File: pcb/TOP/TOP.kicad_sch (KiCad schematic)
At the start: 90 parts

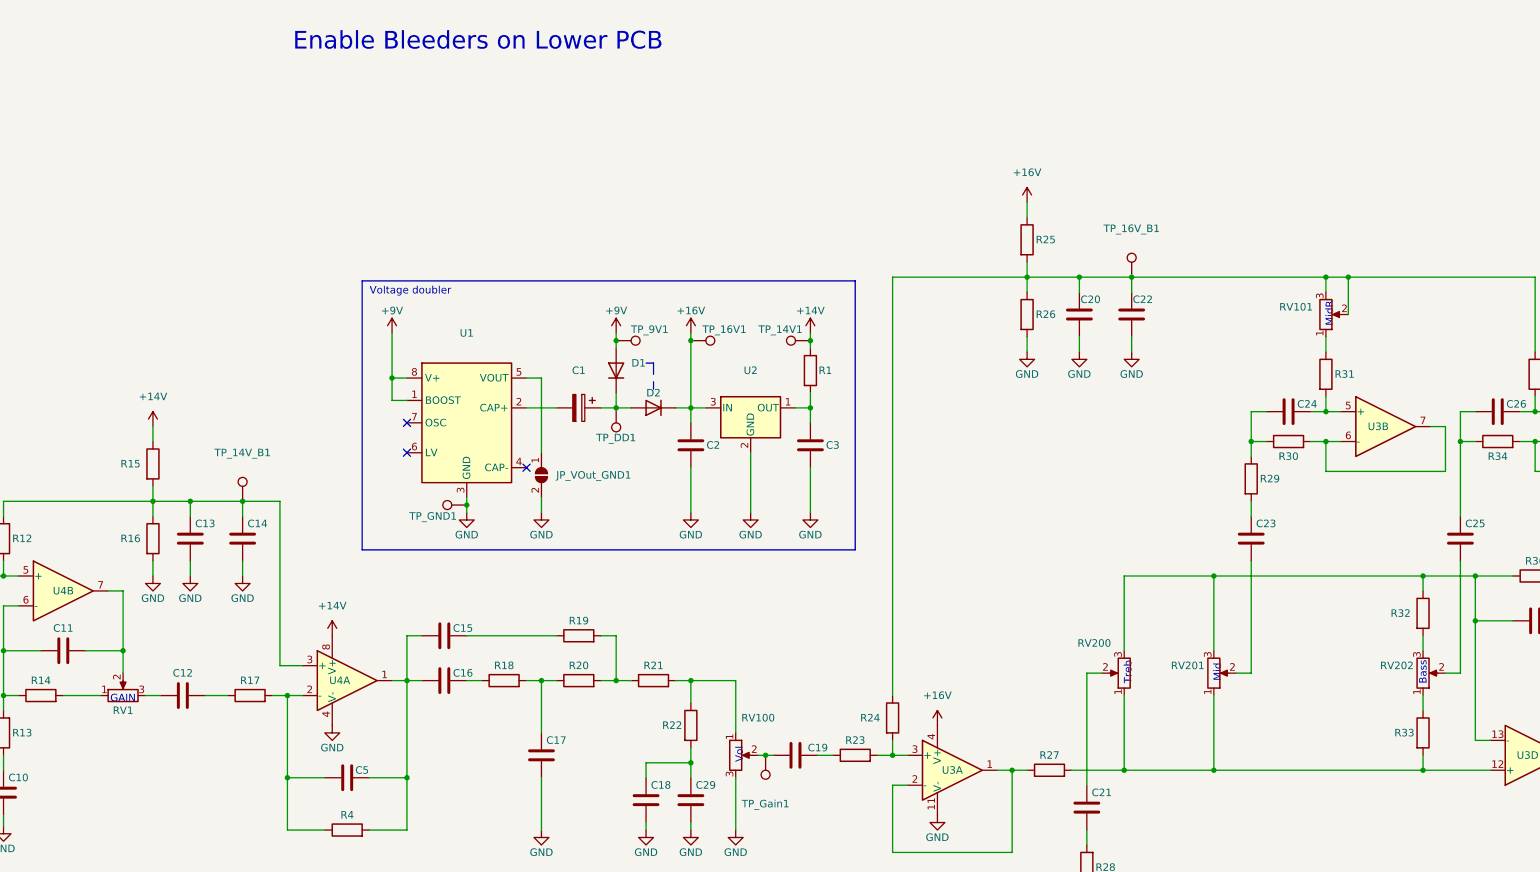
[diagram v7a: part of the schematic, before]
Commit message: [TOP] Consolidate footprints; Add bypass cap to U1
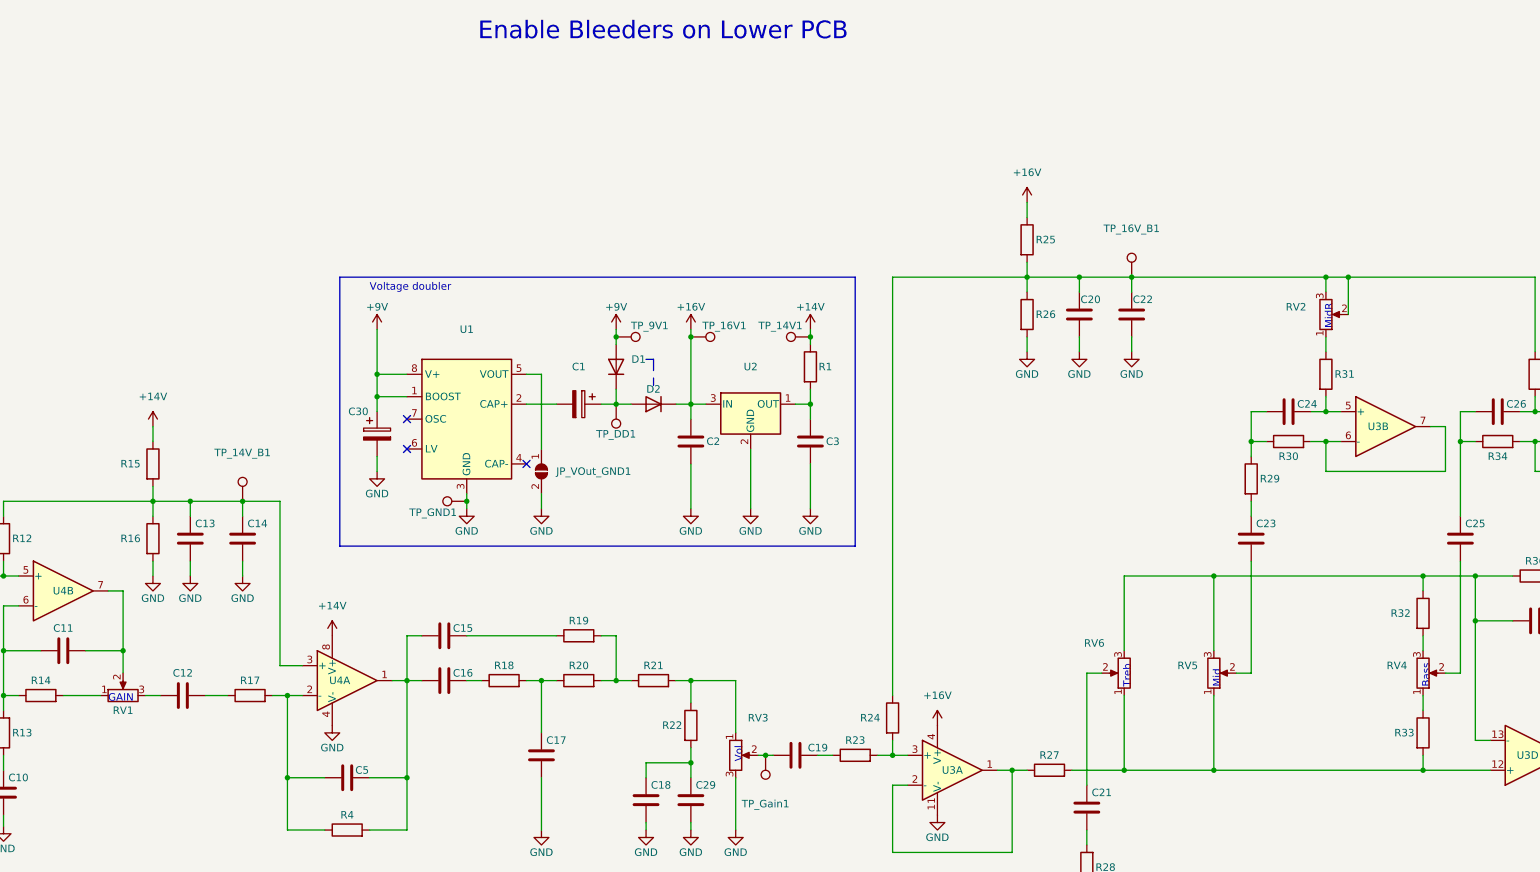
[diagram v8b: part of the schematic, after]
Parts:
- added C30: (no value), symbol Device:C_Polarized
- C1: LCSC C15850 -> C445047
- renumbered RV101 to RV2, RV100 to RV3, RV202 to RV4, RV201 to RV5, RV200 to RV6
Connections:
- net +9V: now also C30.1
- net GND: now also C30.2
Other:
- moved on the sheet: C1, C2, C3, D1, D2, JP_VOut_GND1, R1, TP_14V1, TP_16V1, TP_9V1, TP_DD1, TP_GND1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
